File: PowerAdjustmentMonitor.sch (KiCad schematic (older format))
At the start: 44 parts, among them P6 CONN_1, P7 CONN_1, U11 LM317T, U6 LM337T, U8 LM337T, U9 LM317T

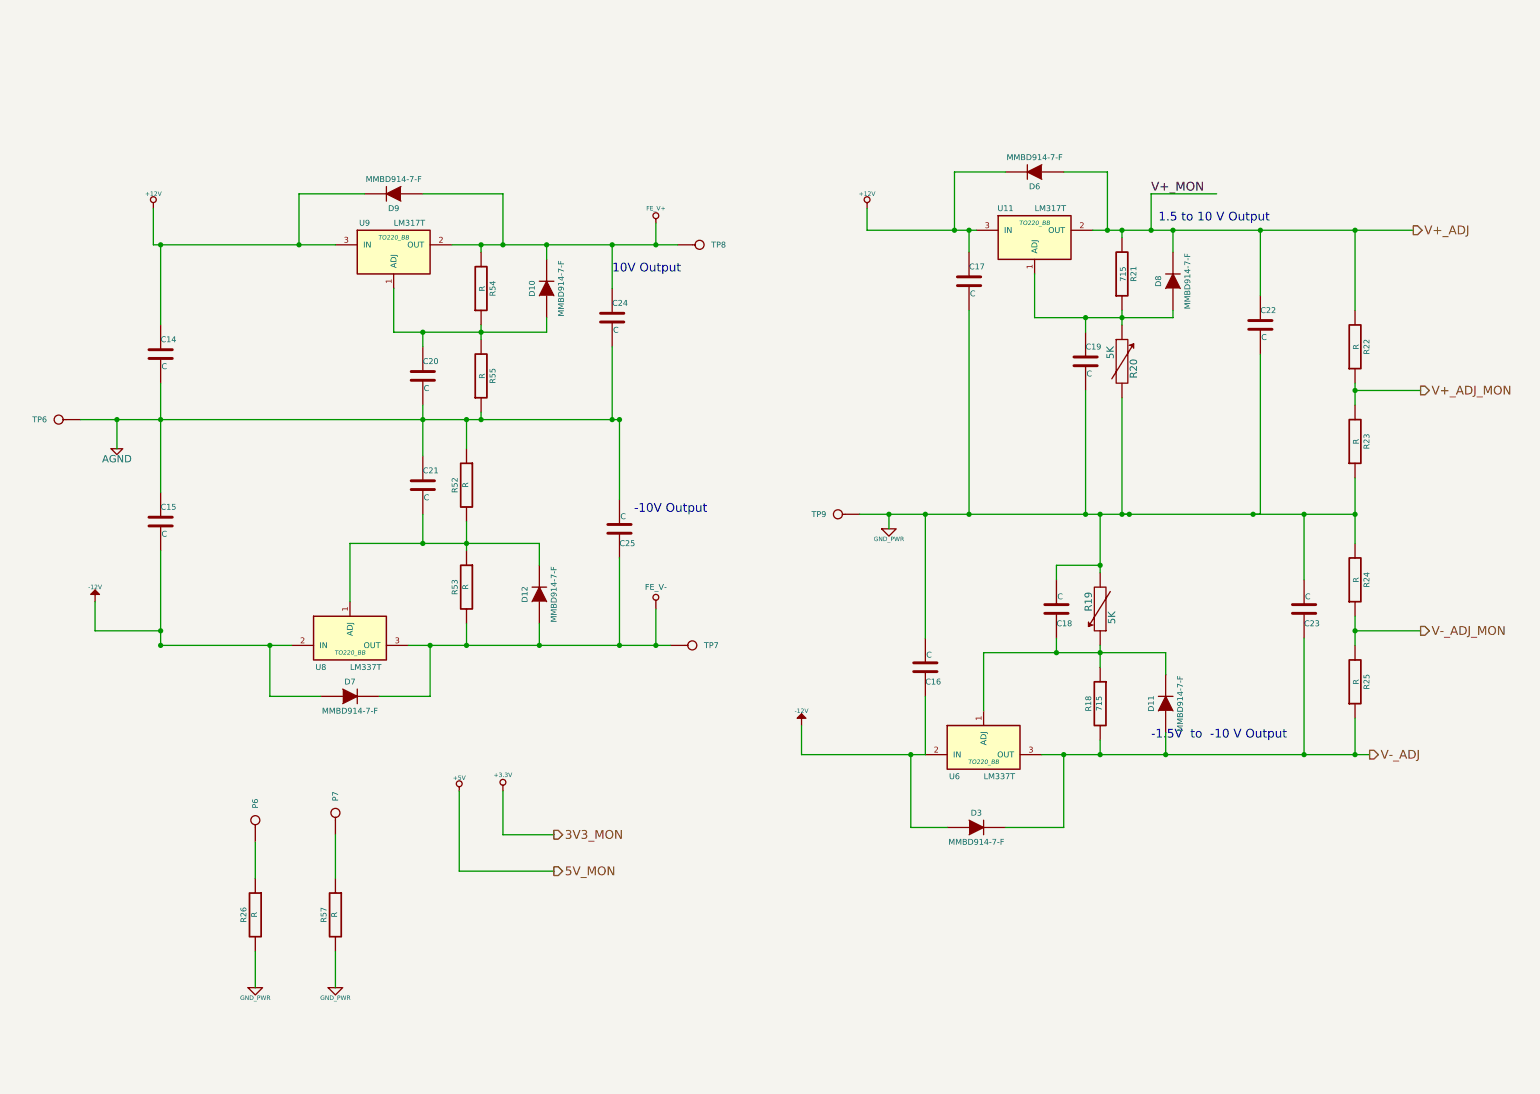
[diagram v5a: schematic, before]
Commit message: Analog IO Cleanup/Additions
Added some placed holder caps and resistors
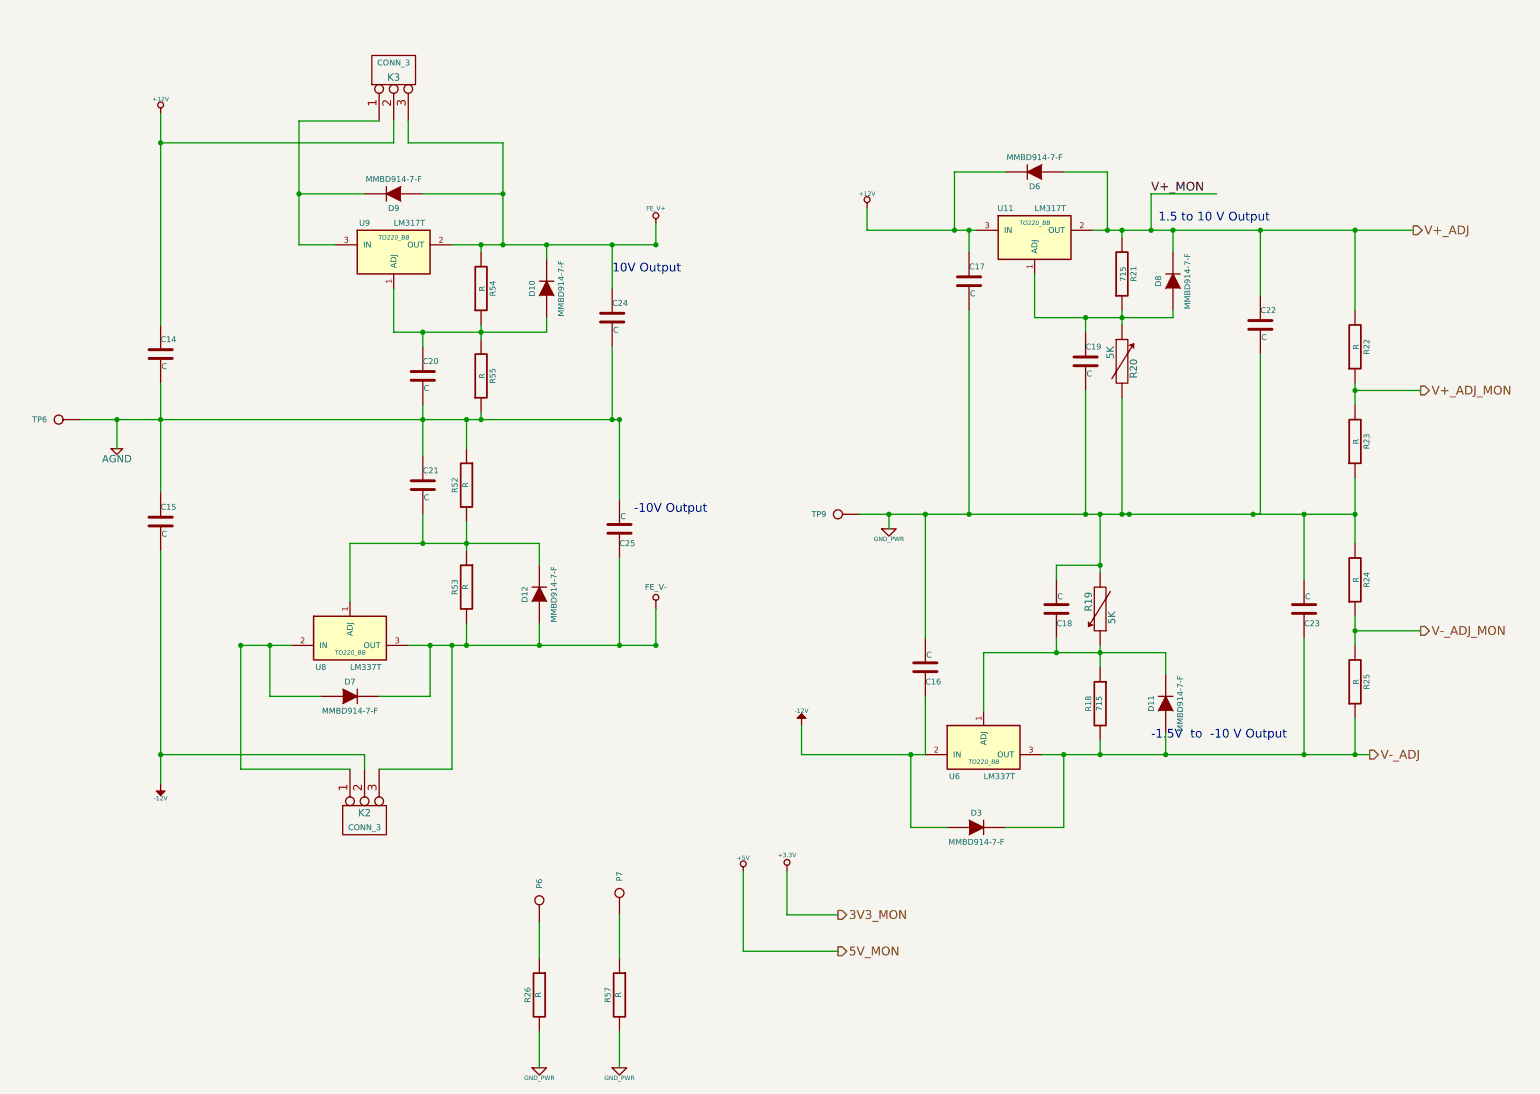
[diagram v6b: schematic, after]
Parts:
- removed TP7: FE_V-, symbol CONN_1
- removed TP8: FE_V+, symbol CONN_1
- added K2, K3: CONN_3, symbol CONN_3
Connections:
- net +12V: now also K3.2 (PM); no longer D9.2 (K), U9.3 (IN)
- net -12V: now also K2.2 (PM); no longer D7.1 (A), U8.2 (IN)
- net FE_V+: now also K3.3 (P3)
- net FE_V-: now also K2.3 (P3)
- new net: D7.1 (A), K2.1 (P1), U8.2 (IN)
- new net: D9.2 (K), K3.1 (P1), U9.3 (IN)
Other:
- moved on the sheet: P6, P7, R26, R57

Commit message: Added Passive Values and SPICE models
As part of week 1 of Session 1B, we added a SPICE model of the In amp
and went through and assigned values to all of the passive components.
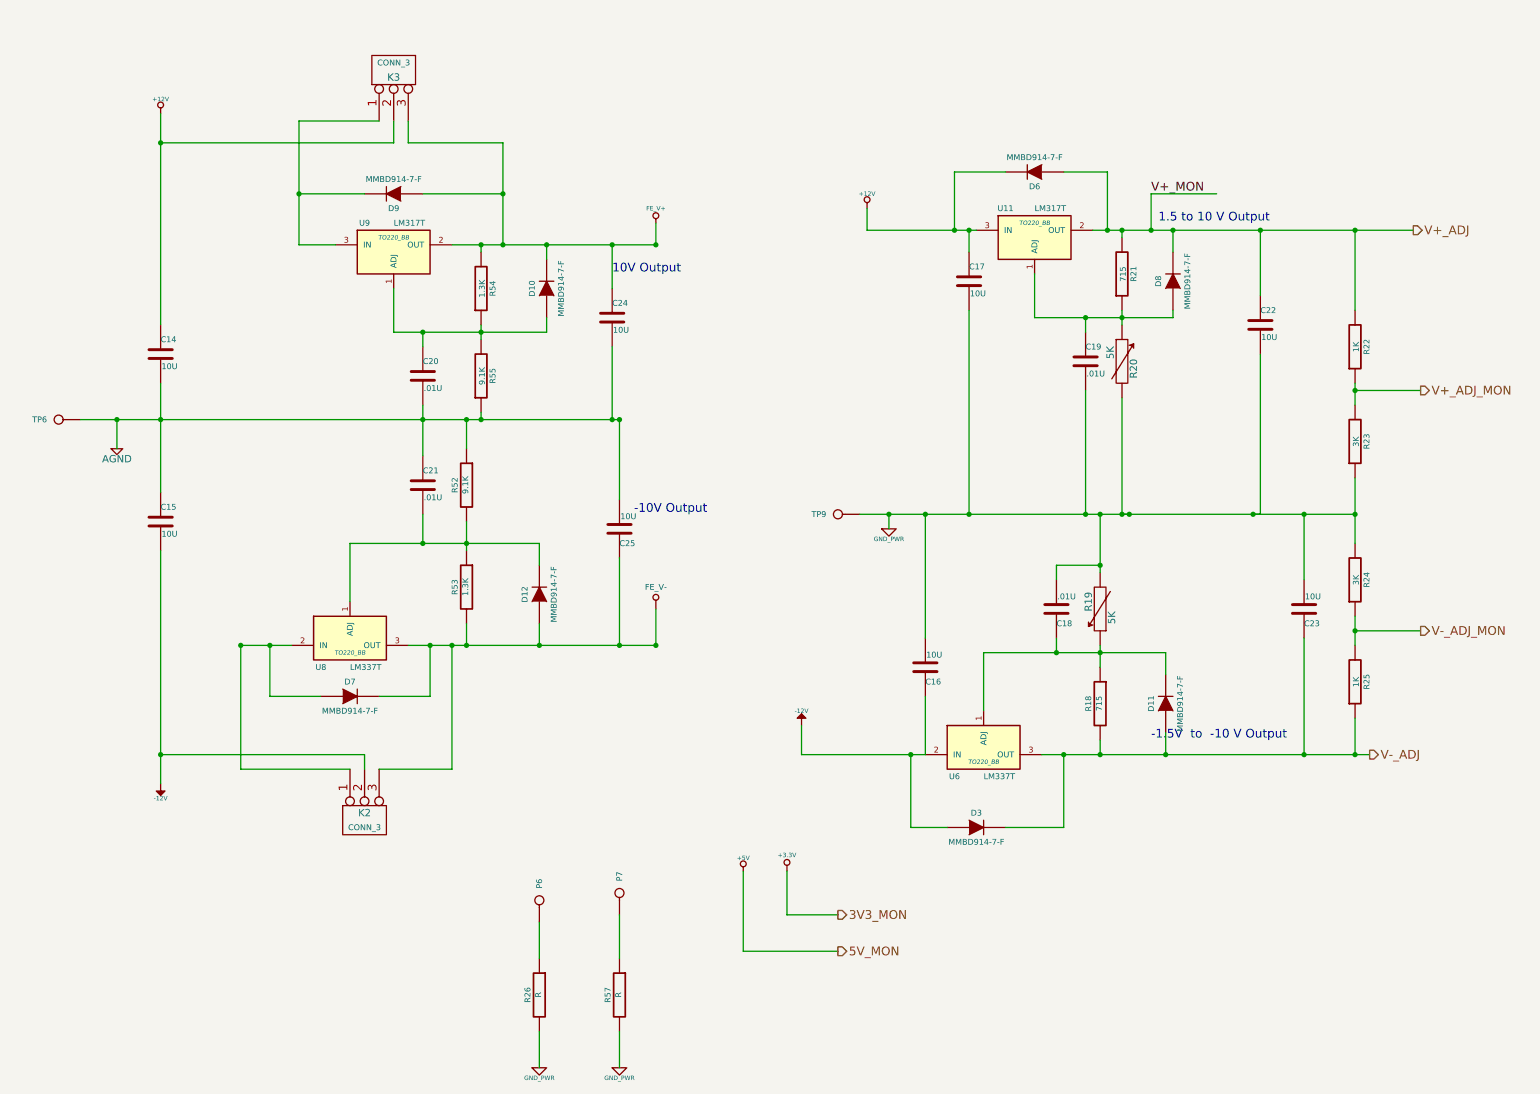
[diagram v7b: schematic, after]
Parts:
- C14, C15, C16, C17, C22, C23, C24, C25: value C -> 10U
- C18, C19, C20, C21: value C -> .01U
- R22, R25: value R -> 1K
- R23, R24: value R -> 3K
- R52, R55: value R -> 9.1K
- R53, R54: value R -> 1.3K
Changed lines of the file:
@@
-EESchema Schematic File Version 2  date 2/16/2014 3:41:32 PM
+EESchema Schematic File Version 2  date 4/16/2014 11:04:06 PM
 LIBS:power
 LIBS:device
@@
 Sheet 5 9
 Title ""
-Date "16 feb 2014"
+Date "17 apr 2014"
 Rev ""
 Comp ""
@@
 P 9750 2650
 F 0 "R22" V 9830 2650 40  0000 C CNN
-F 1 "R" V 9757 2651 40  0000 C CNN
+F 1 "1K" V 9757 2651 40  0000 C CNN
 F 2 "~" V 9680 2650 30  0000 C CNN
 F 3 "~" H 9750 2650 30  0000 C CNN
@@
 P 9750 3300
 F 0 "R23" V 9830 3300 40  0000 C CNN
-F 1 "R" V 9757 3301 40  0000 C CNN
+F 1 "3K" V 9757 3301 40  0000 C CNN
 F 2 "~" V 9680 3300 30  0000 C CNN
 F 3 "~" H 9750 3300 30  0000 C CNN
@@
 P 9750 4250
 F 0 "R24" V 9830 4250 40  0000 C CNN
-F 1 "R" V 9757 4251 40  0000 C CNN
+F 1 "3K" V 9757 4251 40  0000 C CNN
 F 2 "~" V 9680 4250 30  0000 C CNN
 F 3 "~" H 9750 4250 30  0000 C CNN
@@
 P 9750 4950
 F 0 "R25" V 9830 4950 40  0000 C CNN
-F 1 "R" V 9757 4951 40  0000 C CNN
+F 1 "1K" V 9757 4951 40  0000 C CNN
 F 2 "~" V 9680 4950 30  0000 C CNN
 F 3 "~" H 9750 4950 30  0000 C CNN
@@
 P 3750 2850
 F 0 "R55" V 3830 2850 40  0000 C CNN
-F 1 "R" V 3757 2851 40  0000 C CNN
+F 1 "9.1K" V 3757 2851 40  0000 C CNN
 F 2 "~" V 3680 2850 30  0000 C CNN
 F 3 "~" H 3750 2850 30  0000 C CNN
@@
 P 3750 2250
 F 0 "R54" V 3830 2250 40  0000 C CNN
-F 1 "R" V 3757 2251 40  0000 C CNN
+F 1 "1.3K" V 3757 2251 40  0000 C CNN
 F 2 "~" V 3680 2250 30  0000 C CNN
 F 3 "~" H 3750 2250 30  0000 C CNN
@@
 P 3650 3600
 F 0 "R52" V 3730 3600 40  0000 C CNN
-F 1 "R" V 3657 3601 40  0000 C CNN
+F 1 "9.1K" V 3657 3601 40  0000 C CNN
 F 2 "~" V 3580 3600 30  0000 C CNN
 F 3 "~" H 3650 3600 30  0000 C CNN
@@
 P 3650 4300
 F 0 "R53" V 3730 4300 40  0000 C CNN
-F 1 "R" V 3657 4301 40  0000 C CNN
+F 1 "1.3K" V 3657 4301 40  0000 C CNN
 F 2 "~" V 3580 4300 30  0000 C CNN
 F 3 "~" H 3650 4300 30  0000 C CNN
@@
 P 9100 2500
 F 0 "C22" H 9100 2600 40  0000 L CNN
-F 1 "C" H 9106 2415 40  0000 L CNN
+F 1 "10U" H 9106 2415 40  0000 L CNN
 F 2 "~" H 9138 2350 30  0000 C CNN
 F 3 "~" H 9100 2500 60  0000 C CNN
@@
 P 4700 3900
 F 0 "C25" H 4700 4000 40  0000 L CNN
-F 1 "C" H 4706 3815 40  0000 L CNN
+F 1 "10U" H 4706 3815 40  0000 L CNN
 F 2 "~" H 4738 3750 30  0000 C CNN
 F 3 "~" H 4700 3900 60  0000 C CNN
@@
 P 9400 4450
 F 0 "C23" H 9400 4550 40  0000 L CNN
-F 1 "C" H 9406 4365 40  0000 L CNN
+F 1 "10U" H 9406 4365 40  0000 L CNN
 F 2 "~" H 9438 4300 30  0000 C CNN
 F 3 "~" H 9400 4450 60  0000 C CNN
@@
 P 6800 4850
 F 0 "C16" H 6800 4950 40  0000 L CNN
-F 1 "C" H 6806 4765 40  0000 L CNN
+F 1 "10U" H 6806 4765 40  0000 L CNN
 F 2 "~" H 6838 4700 30  0000 C CNN
 F 3 "~" H 6800 4850 60  0000 C CNN
@@
 P 1550 3850
 F 0 "C15" H 1550 3950 40  0000 L CNN
-F 1 "C" H 1556 3765 40  0000 L CNN
+F 1 "10U" H 1556 3765 40  0000 L CNN
 F 2 "~" H 1588 3700 30  0000 C CNN
 F 3 "~" H 1550 3850 60  0000 C CNN
@@
 P 1550 2700
 F 0 "C14" H 1550 2800 40  0000 L CNN
-F 1 "C" H 1556 2615 40  0000 L CNN
+F 1 "10U" H 1556 2615 40  0000 L CNN
 F 2 "~" H 1588 2550 30  0000 C CNN
 F 3 "~" H 1550 2700 60  0000 C CNN
@@
 P 7100 2200
 F 0 "C17" H 7100 2300 40  0000 L CNN
-F 1 "C" H 7106 2115 40  0000 L CNN
+F 1 "10U" H 7106 2115 40  0000 L CNN
 F 2 "~" H 7138 2050 30  0000 C CNN
 F 3 "~" H 7100 2200 60  0000 C CNN
@@
 P 3350 3600
 F 0 "C21" H 3350 3700 40  0000 L CNN
-F 1 "C" H 3356 3515 40  0000 L CNN
+F 1 ".01U" H 3356 3515 40  0000 L CNN
 F 2 "~" H 3388 3450 30  0000 C CNN
 F 3 "~" H 3350 3600 60  0000 C CNN
@@
 P 3350 2850
 F 0 "C20" H 3350 2950 40  0000 L CNN
-F 1 "C" H 3356 2765 40  0000 L CNN
+F 1 ".01U" H 3356 2765 40  0000 L CNN
 F 2 "~" H 3388 2700 30  0000 C CNN
 F 3 "~" H 3350 2850 60  0000 C CNN
@@
 P 7900 2750
 F 0 "C19" H 7900 2850 40  0000 L CNN
-F 1 "C" H 7906 2665 40  0000 L CNN
+F 1 ".01U" H 7906 2665 40  0000 L CNN
 F 2 "~" H 7938 2600 30  0000 C CNN
 F 3 "~" H 7900 2750 60  0000 C CNN
@@
 P 7700 4450
 F 0 "C18" H 7700 4550 40  0000 L CNN
-F 1 "C" H 7706 4365 40  0000 L CNN
+F 1 ".01U" H 7706 4365 40  0000 L CNN
 F 2 "~" H 7738 4300 30  0000 C CNN
 F 3 "~" H 7700 4450 60  0000 C CNN
@@
 P 4650 2450
 F 0 "C24" H 4650 2550 40  0000 L CNN
-F 1 "C" H 4656 2365 40  0000 L CNN
+F 1 "10U" H 4656 2365 40  0000 L CNN
 F 2 "~" H 4688 2300 30  0000 C CNN
 F 3 "~" H 4650 2450 60  0000 C CNN
